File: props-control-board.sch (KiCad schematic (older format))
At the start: 63 parts, among them J1 Conn_01x04_Female, J10 Conn_01x02_Female, J11 Conn_01x02_Female, J12 Conn_01x02_Female, J13 Conn_01x02_Female, J2 Conn_01x03_Female, J3 Conn_01x03_Female, J4 Conn_01x03_Female, J5 Conn_01x06_Female, J6 Conn_01x05_Female, J7 Conn_01x04_Female, J8 Conn_01x02_Female, J9 Conn_01x02_Female, Q1 DMN24H3D5L, Q2 DMN24H3D5L, Q3 DMN24H3D5L, Q4 DMN24H3D5L, Q5 DMN24H3D5L, Q6 DMN24H3D5L, Q7 DMN24H3D5L, Q8 DMN24H3D5L, U1 AZ1117-3.3, U10 HCPL2631SD, U11 RFM-0505S, U2 VOS628A, U3 arduino_pro_mini, U4 STM32F042K6T6, U5 TXB0101DCKT, U6 TXB0104PWR, U7 AZ1117-3.3, U8 SX1278_module, U9 HCPL2631SD, Y1 Crystal_GND24

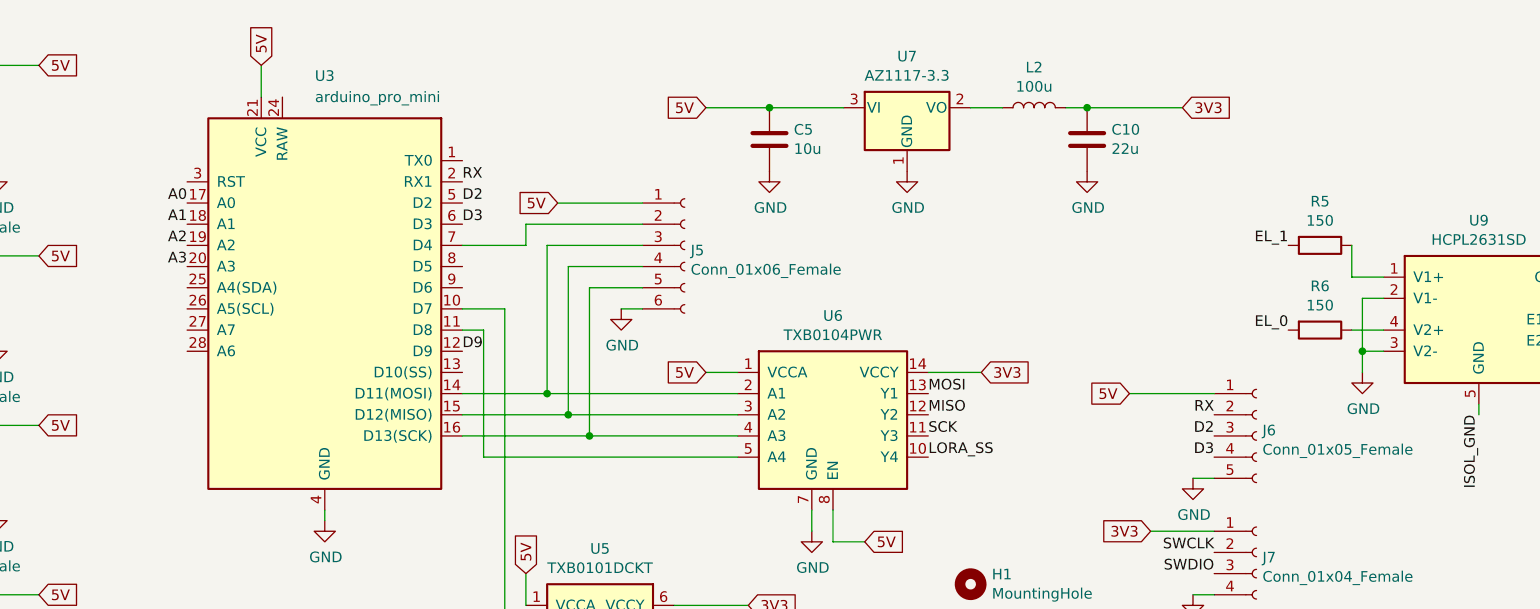
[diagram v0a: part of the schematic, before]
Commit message: expose more GPIO and expose UART
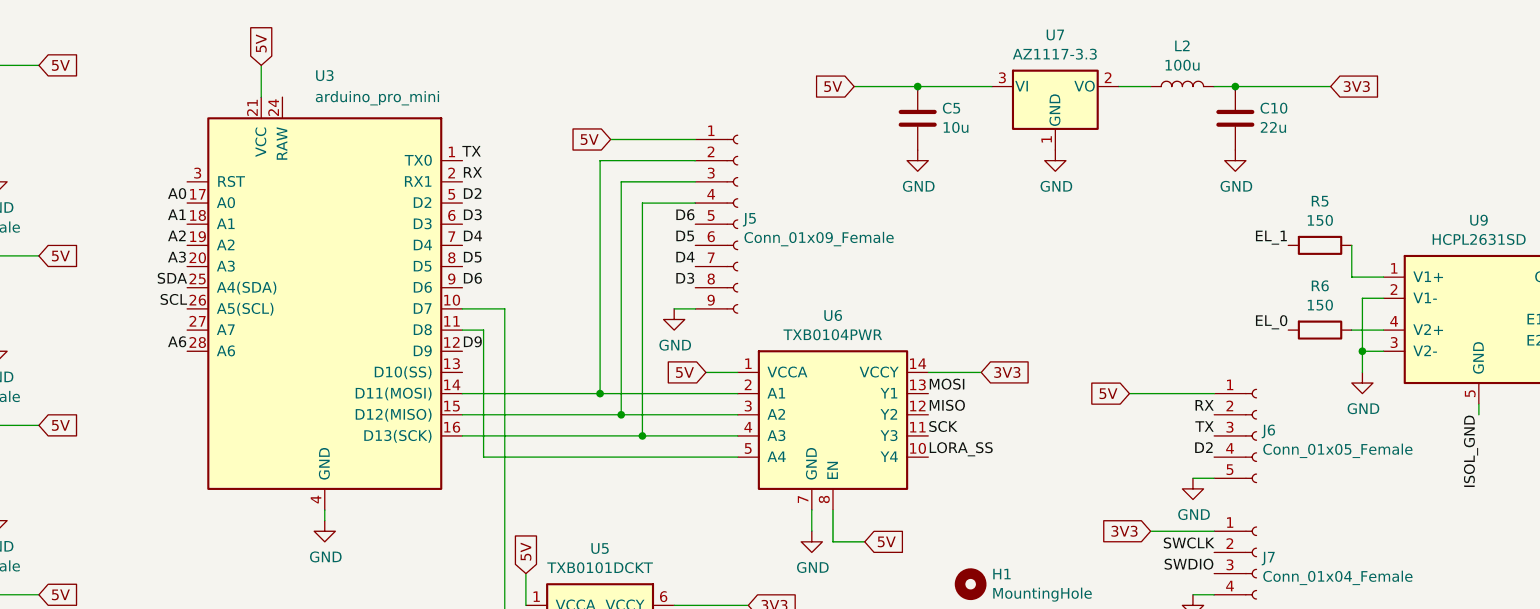
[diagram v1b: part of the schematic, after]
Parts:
- removed J5: Conn_01x06_Female, Connector_JST:JST_XH_B6B-XH-A_1x06_P2.50mm_Vertical, symbol Connector:Conn_01x06_Female
- added J5: Conn_01x09_Female, Connector_JST:JST_XH_B9B-XH-A_1x09_P2.50mm_Vertical, symbol Connector:Conn_01x09_Female
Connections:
- net 5V: now also J5.1 (Pin_1)
- net D2: now also J6.4 (Pin_4); no longer J6.3 (Pin_3)
- net D3: now also J5.8 (Pin_8); no longer J6.4 (Pin_4)
- net GND: now also J5.9 (Pin_9)
- net TX: now reaches U3.1 (TX0)
- net TX: now also J6.3 (Pin_3)
- net at U3.14 (D11(MOSI)), U6.2 (A1): now also J5.2 (Pin_2)
- net at U3.15 (D12(MISO)), U6.3 (A2): now also J5.3 (Pin_3)
- net at U3.16 (D13(SCK)), U6.4 (A3): now also J5.4 (Pin_4)
- net SDA: now reaches U3.25 (A4(SDA))
- net SCL: now reaches U3.26 (A5(SCL))
- net A6: now reaches U3.28 (A6)
- net D4: now reaches U3.7 (D4)
- net D4: now also J5.7 (Pin_7)
- net D5: now reaches U3.8 (D5)
- net D5: now also J5.6 (Pin_6)
- net D6: now reaches U3.9 (D6)
- net D6: now also J5.5 (Pin_5)
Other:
- moved on the sheet: C10, C5, L2, U7

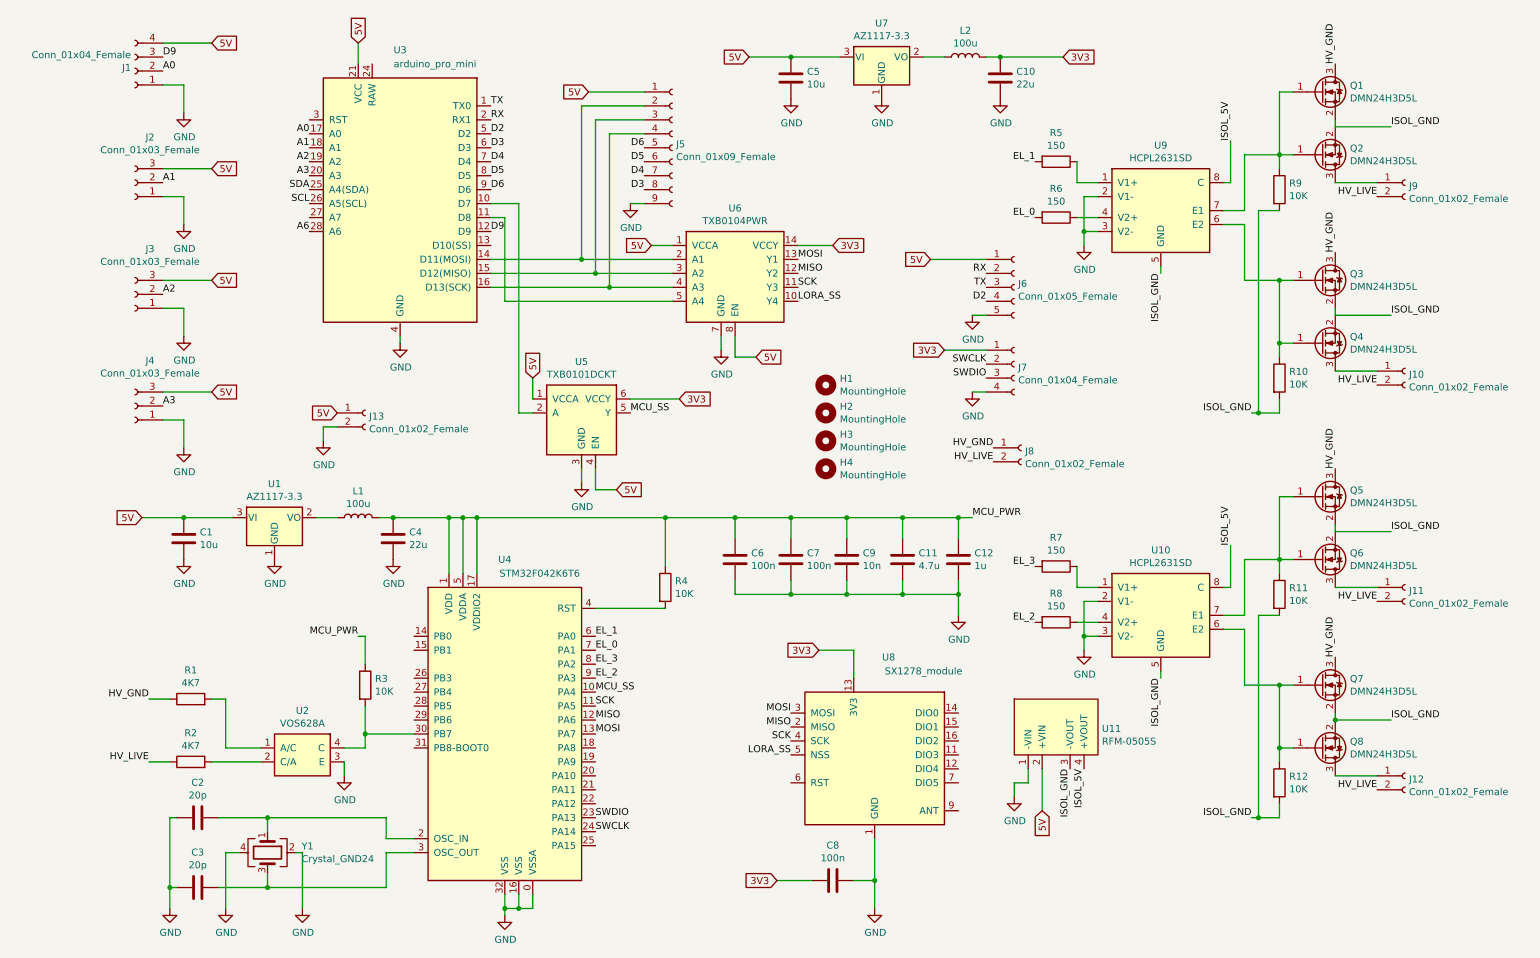
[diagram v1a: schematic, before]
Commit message: add reset connection to LoRa, add antenna connector
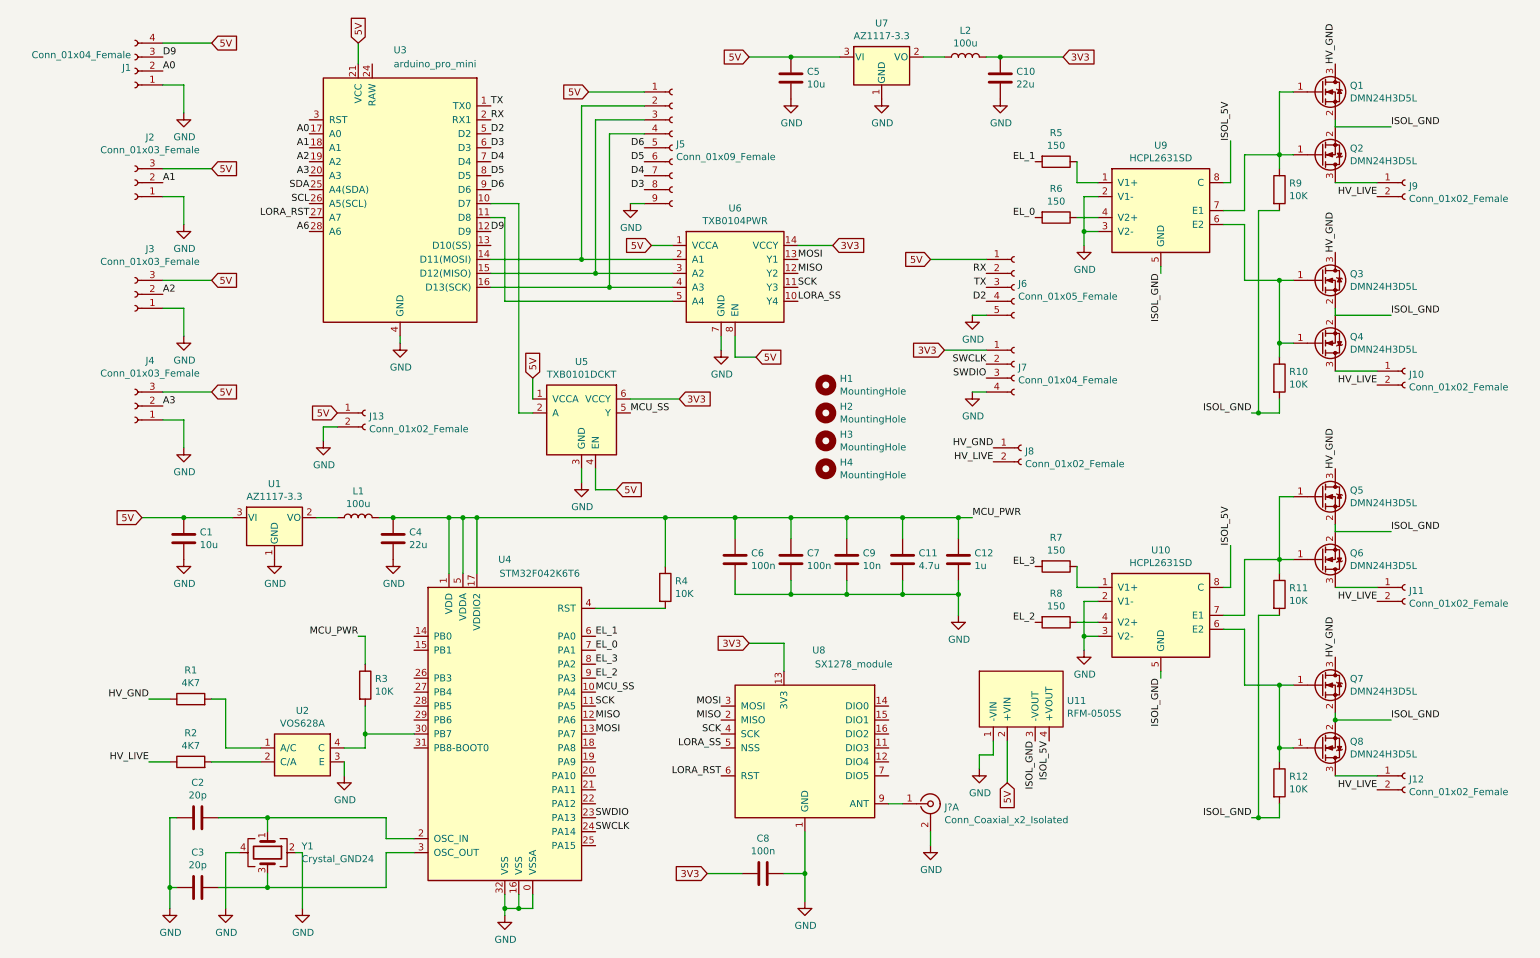
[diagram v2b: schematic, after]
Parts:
- added J?: Conn_Coaxial_x2_Isolated, Connector_Coaxial:U.FL_Hirose_U.FL-R-SMT-1_Vertical, symbol Connector:Conn_Coaxial_x2_Isolated
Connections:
- net GND: now also J?.2 (Ext1)
- net LORA_RST: now reaches U3.27 (A7)
- net LORA_RST: now also U8.6 (RST)
- net at U8.9 (ANT): now also J?.1 (In1)
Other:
- moved on the sheet: C8, U11, U8
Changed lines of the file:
@@
 Text GLabel 6100 2250 2    50   Input ~ 0
 3V3
-Text GLabel 6000 5150 0    50   Input ~ 0
+Text GLabel 5500 5100 0    50   Input ~ 0
 3V3
 Wire Wire Line
-	6000 5150 6250 5150
-Wire Wire Line
-	6250 5150 6250 5350
+	5500 5100 5750 5100
+Wire Wire Line
+	5750 5100 5750 5300
 $Comp
 L power:GND #PWR019
 U 1 1 5FB64920
-P 6400 7000
-F 0 "#PWR019" H 6400 6750 50  0001 C CNN
-F 1 "GND" H 6405 6827 50  0000 C CNN
-F 2 "" H 6400 7000 50  0001 C CNN
-F 3 "" H 6400 7000 50  0001 C CNN
-	1    6400 7000
-	1    0    0    -1
-$EndComp
-Wire Wire Line
-	6400 6800 6400 6500
-Text GLabel 5700 6800 0    50   Input ~ 0
+P 5900 6950
+F 0 "#PWR019" H 5900 6700 50  0001 C CNN
+F 1 "GND" H 5905 6777 50  0000 C CNN
+F 2 "" H 5900 6950 50  0001 C CNN
+F 3 "" H 5900 6950 50  0001 C CNN
+	1    5900 6950
+	1    0    0    -1
+$EndComp
+Wire Wire Line
+	5900 6750 5900 6450
+Text GLabel 5200 6750 0    50   Input ~ 0
 3V3
 Wire Wire Line
-	5700 6800 5950 6800
-Wire Wire Line
-	6250 6800 6400 6800
-Wire Wire Line
-	6400 6800 6400 7000
-Connection ~ 6400 6800
+	5200 6750 5450 6750
+Wire Wire Line
+	5750 6750 5900 6750
+Wire Wire Line
+	5900 6750 5900 6950
+Connection ~ 5900 6750
 Text GLabel 1650 800  2    50   Input ~ 0
 5V
@@
 Text GLabel 5000 3350 2    50   Input ~ 0
 3V3
-Text Label 5800 5600 2    50   ~ 0
+Text Label 5300 5550 2    50   ~ 0
 MOSI
-Text Label 5800 5700 2    50   ~ 0
+Text Label 5300 5650 2    50   ~ 0
 MISO
-Text Label 5800 5800 2    50   ~ 0
+Text Label 5300 5750 2    50   ~ 0
 SCK
-Text Label 5800 5900 2    50   ~ 0
+Text Label 5300 5850 2    50   ~ 0
 LORA_SS
 Text Label 4400 6350 0    50   ~ 0
@@
 D9
 Wire Wire Line
-	7600 6300 7600 6000
-Text GLabel 7600 6300 3    50   Input ~ 0
+	7350 6100 7350 5800
+Text GLabel 7350 6100 3    50   Input ~ 0
 5V
 $Comp
 L power:GND #PWR026
 U 1 1 5FCEB723
-P 7400 6200
-F 0 "#PWR026" H 7400 5950 50  0001 C CNN
-F 1 "GND" H 7405 6027 50  0000 C CNN
-F 2 "" H 7400 6200 50  0001 C CNN
-F 3 "" H 7400 6200 50  0001 C CNN
-	1    7400 6200
-	1    0    0    -1
-$EndComp
-Wire Wire Line
-	7400 6100 7400 6200
-Wire Wire Line
-	7500 6000 7500 6100
-Wire Wire Line
-	7500 6100 7400 6100
-Text Label 7800 6000 3    50   ~ 0
+P 7150 6000
+F 0 "#PWR026" H 7150 5750 50  0001 C CNN
+F 1 "GND" H 7155 5827 50  0000 C CNN
+F 2 "" H 7150 6000 50  0001 C CNN
+F 3 "" H 7150 6000 50  0001 C CNN
+	1    7150 6000
+	1    0    0    -1
+$EndComp
+Wire Wire Line
+	7150 5900 7150 6000
+Wire Wire Line
+	7250 5800 7250 5900
+Wire Wire Line
+	7250 5900 7150 5900
+Text Label 7550 5800 3    50   ~ 0
 ISOL_GND
-Text Label 7900 6000 3    50   ~ 0
+Text Label 7650 5800 3    50   ~ 0
 ISOL_5V
 Text Label 9100 6350 2    50   ~ 0
@@
 L props-control-board:SX1278_module U8
 U 1 1 5FB4A5F0
-P 6400 5850
-F 0 "U8" H 6500 6500 50  0000 C CNN
-F 1 "SX1278_module" H 6750 6400 50  0000 C CNN
-F 2 "props-control-board:SX1278_module" H 6400 5850 50  0001 C CNN
-F 3 "" H 6400 5850 50  0001 C CNN
-	1    6400 5850
+P 5900 5800
+F 0 "U8" H 6000 6450 50  0000 C CNN
+F 1 "SX1278_module" H 6250 6350 50  0000 C CNN
+F 2 "props-control-board:SX1278_module" H 5900 5800 50  0001 C CNN
+F 3 "" H 5900 5800 50  0001 C CNN
+	1    5900 5800
 	1    0    0    -1
 $EndComp
@@
 L Device:C C8
 U 1 1 5FB66124
-P 6100 6800
-F 0 "C8" V 5848 6800 50  0000 C CNN
-F 1 "100n" V 5939 6800 50  0000 C CNN
-F 2 "Capacitor_SMD:C_0603_1608Metric_Pad1.05x0.95mm_HandSolder" H 6138 6650 50  0001 C CNN
-F 3 "~" H 6100 6800 50  0001 C CNN
-F 4 "1276-CL10B104KB8NNNLCT-ND" H 6100 6800 50  0001 C CNN "Digikey Part Number"
-	1    6100 6800
+P 5600 6750
+F 0 "C8" V 5348 6750 50  0000 C CNN
+F 1 "100n" V 5439 6750 50  0000 C CNN
+F 2 "Capacitor_SMD:C_0603_1608Metric_Pad1.05x0.95mm_HandSolder" H 5638 6600 50  0001 C CNN
+F 3 "~" H 5600 6750 50  0001 C CNN
+F 4 "1276-CL10B104KB8NNNLCT-ND" H 5600 6750 50  0001 C CNN "Digikey Part Number"
+	1    5600 6750
 	0    1    1    0
 $EndComp
@@
 L props-control-board:RFM-0505S U11
 U 1 1 5FCC7831
-P 7700 5650
-F 0 "U11" H 8028 5588 50  0000 L CNN
-F 1 "RFM-0505S" H 8028 5497 50  0000 L CNN
-F 2 "props-control-board:RFM-0505S" H 7700 5900 50  0001 C CNN
-F 3 "https://www.recom-power.com/pdf/Econoline/RFM.pdf" H 7700 5900 50  0001 C CNN
-F 4 "945-3159-ND" H 7700 5650 50  0001 C CNN "Digikey Part Number"
-	1    7700 5650
+P 7450 5450
+F 0 "U11" H 7778 5388 50  0000 L CNN
+F 1 "RFM-0505S" H 7778 5297 50  0000 L CNN
+F 2 "props-control-board:RFM-0505S" H 7450 5700 50  0001 C CNN
+F 3 "https://www.recom-power.com/pdf/Econoline/RFM.pdf" H 7450 5700 50  0001 C CNN
+F 4 "945-3159-ND" H 7450 5450 50  0001 C CNN "Digikey Part Number"
+	1    7450 5450
 	1    0    0    -1
 $EndComp
@@
 	1    0    0    -1
 $EndComp
+$Comp
+L Connector:Conn_Coaxial_x2_Isolated J?
+U 1 1 5FECB519
+P 6800 6250
+F 0 "J?" H 6900 6225 50  0000 L CNN
+F 1 "Conn_Coaxial_x2_Isolated" H 6900 6134 50  0000 L CNN
+F 2 "Connector_Coaxial:U.FL_Hirose_U.FL-R-SMT-1_Vertical" H 6800 6250 50  0001 C CNN
+F 3 " ~" H 6800 6250 50  0001 C CNN
+	1    6800 6250
+	1    0    0    -1
+$EndComp
+Wire Wire Line
+	6500 6250 6600 6250
+$Comp
+L power:GND #PWR?
+U 1 1 5FF0C274
+P 6800 6550
+F 0 "#PWR?" H 6800 6300 50  0001 C CNN
+F 1 "GND" H 6805 6377 50  0000 C CNN
+F 2 "" H 6800 6550 50  0001 C CNN
+F 3 "" H 6800 6550 50  0001 C CNN
+	1    6800 6550
+	1    0    0    -1
+$EndComp
+Wire Wire Line
+	6800 6450 6800 6550
+Text Label 5300 6050 2    50   ~ 0
+LORA_RST
+Text Label 2350 2050 2    50   ~ 0
+LORA_RST
 $EndSCHEMATC

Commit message: update pcb
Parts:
- gave numbers to parts that had none: 1
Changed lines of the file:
@@
 $EndComp
 $Comp
-L Connector:Conn_Coaxial_x2_Isolated J?
+L Connector:Conn_Coaxial_x2_Isolated J14
 U 1 1 5FECB519
 P 6800 6250
-F 0 "J?" H 6900 6225 50  0000 L CNN
+F 0 "J14" H 6900 6225 50  0000 L CNN
 F 1 "Conn_Coaxial_x2_Isolated" H 6900 6134 50  0000 L CNN
 F 2 "Connector_Coaxial:U.FL_Hirose_U.FL-R-SMT-1_Vertical" H 6800 6250 50  0001 C CNN
@@
 	6500 6250 6600 6250
 $Comp
-L power:GND #PWR?
+L power:GND #PWR0103
 U 1 1 5FF0C274
 P 6800 6550
-F 0 "#PWR?" H 6800 6300 50  0001 C CNN
+F 0 "#PWR0103" H 6800 6300 50  0001 C CNN
 F 1 "GND" H 6805 6377 50  0000 C CNN
 F 2 "" H 6800 6550 50  0001 C CNN
